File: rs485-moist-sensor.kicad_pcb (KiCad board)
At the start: 2 copper layers, 18 x 149 mm, 33 parts, among them IC1 ATTINY441-SSU, P1 CONN_02X03, P2 CONN_01X04, Q1 Q_PMOS_GSD, U1 SN65HVD72, U2 MCP1702, X1 16MHz

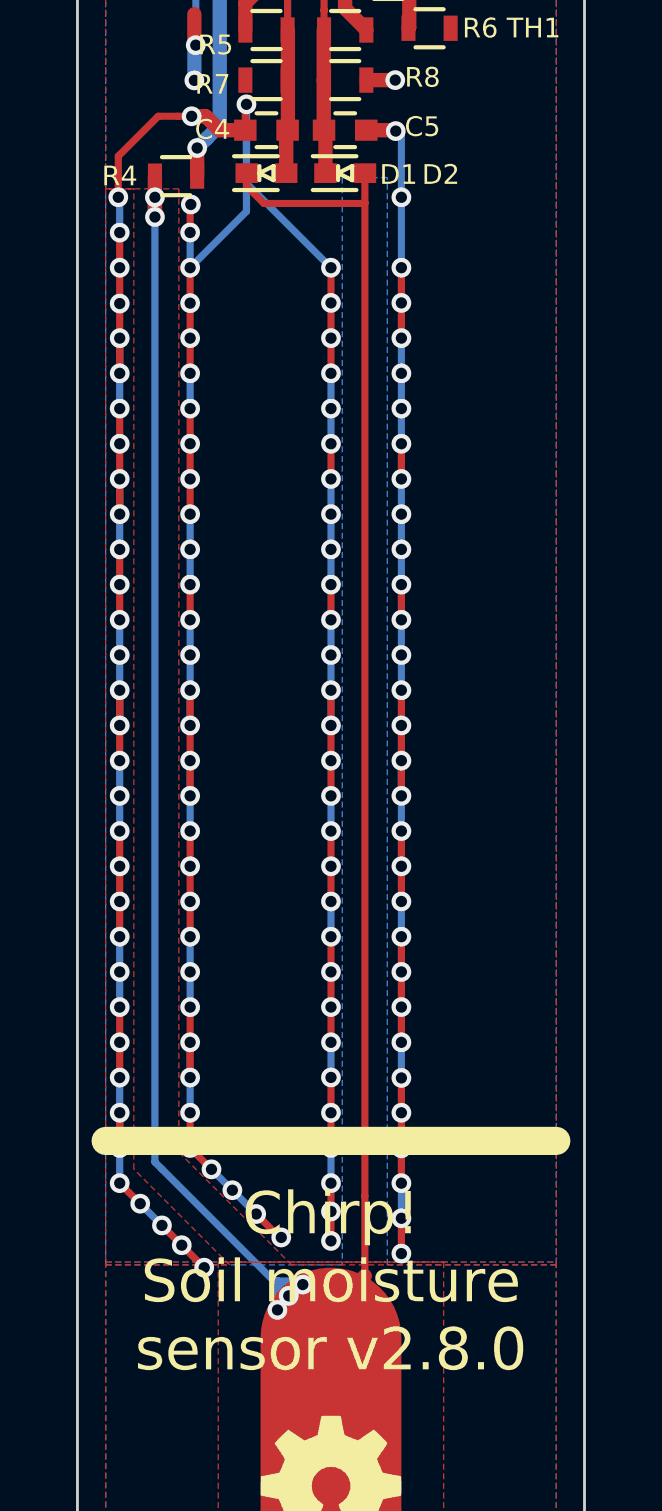
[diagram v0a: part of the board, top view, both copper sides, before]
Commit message: 4 layer configuration
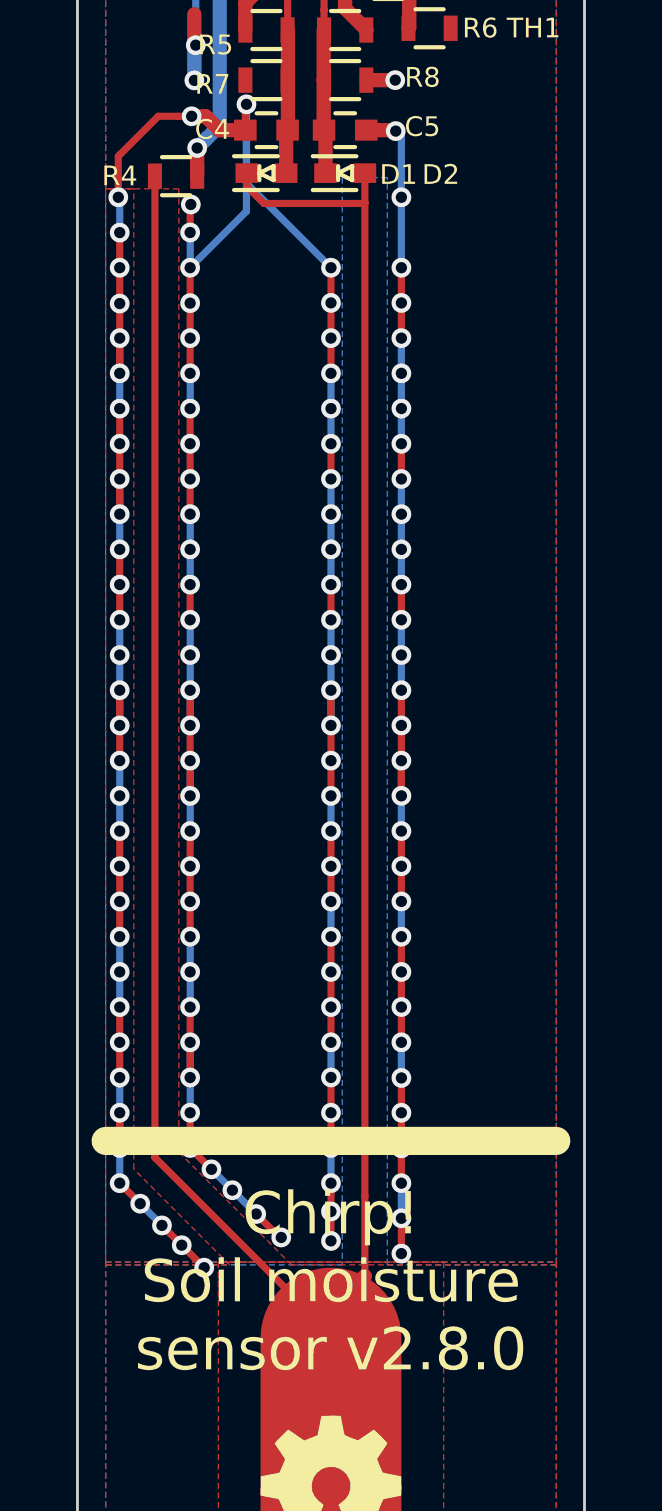
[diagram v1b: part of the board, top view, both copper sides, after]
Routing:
- net /SENSOR_TRACK: track 145.2 -> 140.0 mm, vias 5 -> 0
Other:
- copper layers 2 -> 4
- board text removed: "Catnip Electronics mic@wemakethings.net https://github.com/Miceuz/rs485-moist-sensor"
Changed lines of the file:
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@@
   (general
     (thickness 1.6)
-    (drawings 17)
-    (tracks 580)
+    (drawings 16)
+    (tracks 562)
     (zones 0)
     (modules 33)
@@
   (layers
     (0 F.Cu signal)
+    (1 In1.Cu signal)
+    (2 In2.Cu signal)
     (31 B.Cu signal)
     (32 B.Adhes user)
     (33 F.Adhes user)
-    (34 B.Paste user)
+    (34 B.Paste user hide)
     (35 F.Paste user)
-    (36 B.SilkS user hide)
-    (37 F.SilkS user)
+    (36 B.SilkS user)
+    (37 F.SilkS user hide)
     (38 B.Mask user)
     (39 F.Mask user)
@@
     (46 B.CrtYd user)
     (47 F.CrtYd user)
-    (48 B.Fab user hide)
+    (48 B.Fab user)
     (49 F.Fab user hide)
   )
@@
     (edge_width 0.1)
     (segment_width 0.2)
-    (pcb_text_width 0.3)
+    (pcb_text_width 0.175)
     (pcb_text_size 0.7 0.7)
     (mod_edge_width 0.15)
@@
     (uvia_dia 0.508)
     (uvia_drill 0.127)
+    (diff_pair_width 0.254)
+    (diff_pair_gap 0.25)
     (add_net +3V3)
     (add_net /EXCITATION)
@@
     (uvia_dia 0.508)
     (uvia_drill 0.127)
+    (diff_pair_width 0.254)
+    (diff_pair_gap 0.25)
     (add_net /SENSOR_TRACK)
   )
@@
     (uvia_dia 0.508)
     (uvia_drill 0.127)
+    (diff_pair_width 0.254)
+    (diff_pair_gap 0.25)
   )
   (module Crystals:Crystal_SMD_3225-4pin_3.2x2.5mm (layer F.Cu)
@@
   (gr_line (start 86 21) (end 90 13) (layer Edge.Cuts) (width 0.1))
   (gr_line (start 104 21) (end 100 13) (layer Edge.Cuts) (width 0.1))
-  (gr_text "Catnip Electronics\nmic@wemakethings.net\nhttps://github.com/Miceuz/rs485-moist-sensor" (at 95 124.25 90) (layer B.SilkS)
-    (effects (font (size 1.5 1.5) (thickness 0.3)) (justify mirror))
-  )
   (gr_line (start 87 91) (end 103 91) (layer B.SilkS) (width 1))
   (gr_line (start 87 91) (end 103 91) (layer F.SilkS) (width 1))
@@
   (segment (start 96.204 56.642) (end 96.204 57.7) (width 0.254) (layer F.Cu) (net 6))
   (segment (start 96.204 57.7) (end 96.204 92.959962) (width 0.254) (layer F.Cu) (net 6))
-  (segment (start 94 96.099994) (end 93.100006 96.099994) (width 0.508) (layer B.Cu) (net 6))
-  (segment (start 93.100006 96.099994) (end 93.1 96.1) (width 0.508) (layer B.Cu) (net 6))
-  (segment (start 89 92) (end 93.1 96.1) (width 0.254) (layer B.Cu) (net 6))
-  (segment (start 93.1 96.1) (end 93.5 96.5) (width 0.254) (layer B.Cu) (net 6))
-  (segment (start 93.1 97) (end 93.1 96.505026) (width 0.508) (layer B.Cu) (net 6))
-  (segment (start 93.1 96.505026) (end 93.1 96.1) (width 0.508) (layer B.Cu) (net 6))
-  (segment (start 93.900006 96.099994) (end 94 96.099994) (width 0.508) (layer B.Cu) (net 6))
-  (segment (start 93.5 96.5) (end 93.900006 96.099994) (width 0.508) (layer B.Cu) (net 6))
-  (via (at 94 96.099994) (size 0.7) (drill 0.4) (layers F.Cu B.Cu) (net 6))
-  (segment (start 93.1 96.9) (end 93.1 97) (width 0.508) (layer F.Cu) (net 6))
-  (segment (start 93.5 96.5) (end 93.1 96.9) (width 0.508) (layer F.Cu) (net 6))
-  (via (at 93.1 97) (size 0.7) (drill 0.4) (layers F.Cu B.Cu) (net 6))
-  (segment (start 88.75 56.75) (end 88.75 58.2) (width 0.508) (layer F.Cu) (net 6))
-  (segment (start 88.75 57.5) (end 88.75 58.2) (width 0.508) (layer B.Cu) (net 6))
-  (via (at 88.75 58.2) (size 0.7) (drill 0.4) (layers F.Cu B.Cu) (net 6))
-  (segment (start 88.75 91.75) (end 89 92) (width 0.254) (layer B.Cu) (net 6))
-  (segment (start 93.5 96.5) (end 95 98) (width 0.254) (layer F.Cu) (net 6))
   (segment (start 96.204 95.796) (end 94.128468 97.871532) (width 0.508) (layer F.Cu) (net 6))
   (segment (start 96.204 92.959962) (end 96.204 95.796) (width 0.254) (layer F.Cu) (net 6))
@@
   (segment (start 95 98) (end 94.256936 98) (width 0.508) (layer F.Cu) (net 6))
   (segment (start 94.256936 98) (end 94.128468 97.871532) (width 0.508) (layer F.Cu) (net 6))
-  (segment (start 88.75 57.5) (end 88.75 91.75) (width 0.254) (layer B.Cu) (net 6))
-  (via (at 93.5 96.5) (size 0.7) (drill 0.4) (layers F.Cu B.Cu) (net 6))
-  (segment (start 88.75 56.75) (end 88.75 57.5) (width 0.254) (layer F.Cu) (net 6))
-  (via (at 88.75 57.5) (size 0.7) (drill 0.4) (layers F.Cu B.Cu) (net 6))
   (segment (start 95 98) (end 95 146) (width 5) (layer F.Cu) (net 6))
+  (segment (start 95 97.843962) (end 95 98) (width 0.254) (layer F.Cu) (net 6))
+  (segment (start 88.75 91.593962) (end 95 97.843962) (width 0.254) (layer F.Cu) (net 6))
+  (segment (start 88.75 56.75) (end 88.75 91.593962) (width 0.254) (layer F.Cu) (net 6))
   (segment (start 97.778 49.784) (end 97.778 51.472) (width 0.508) (layer F.Cu) (net 7))
   (segment (start 97.778 51.472) (end 97.75 51.5) (width 0.508) (layer F.Cu) (net 7))

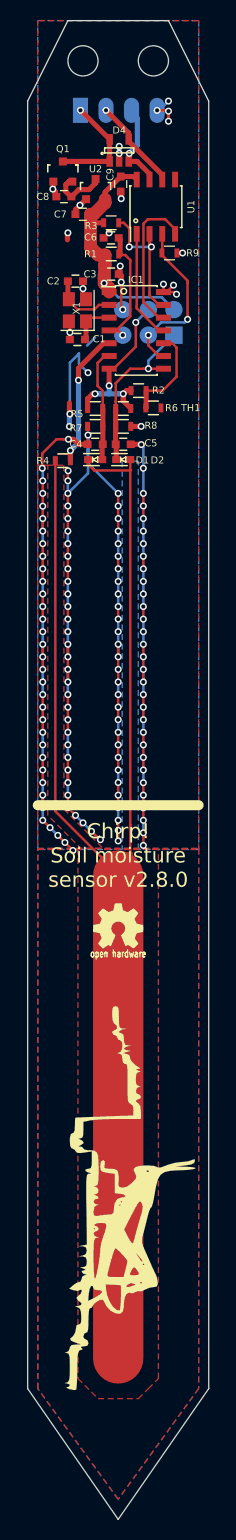
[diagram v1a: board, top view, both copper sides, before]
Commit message: GND into inner layers
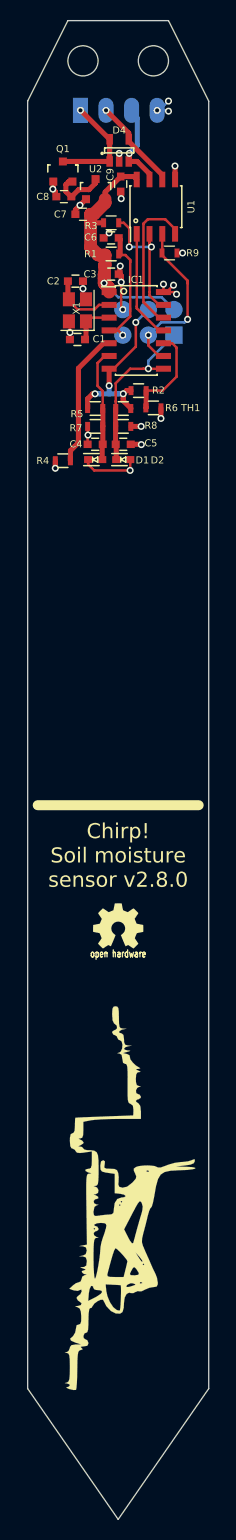
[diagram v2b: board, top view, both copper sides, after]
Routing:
- net GND: track 225.8 -> 27.8 mm, vias 151 -> 22
- net /SENSOR_TRACK: track 140.0 -> 139.2 mm, vias 0 -> 2
- net /EXCITATION: vias 2 -> 0
- added copper zone on In1.Cu, net GND
- added copper zone on In2.Cu, net GND
- removed copper zone on B.Cu, net GND
- removed copper zone on F.Cu, net GND
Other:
- board text added: "Catnip Electronics mic@wemakethings.net https://github.com/Miceuz/rs485-moist-sensor"
